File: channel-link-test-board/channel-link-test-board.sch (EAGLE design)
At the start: 60 parts, among them U1 DS90CR217MTD/NOPBMTD48_TEX-L, U2 DS90CR218AMTD/NOPBMTD48_TEX-L

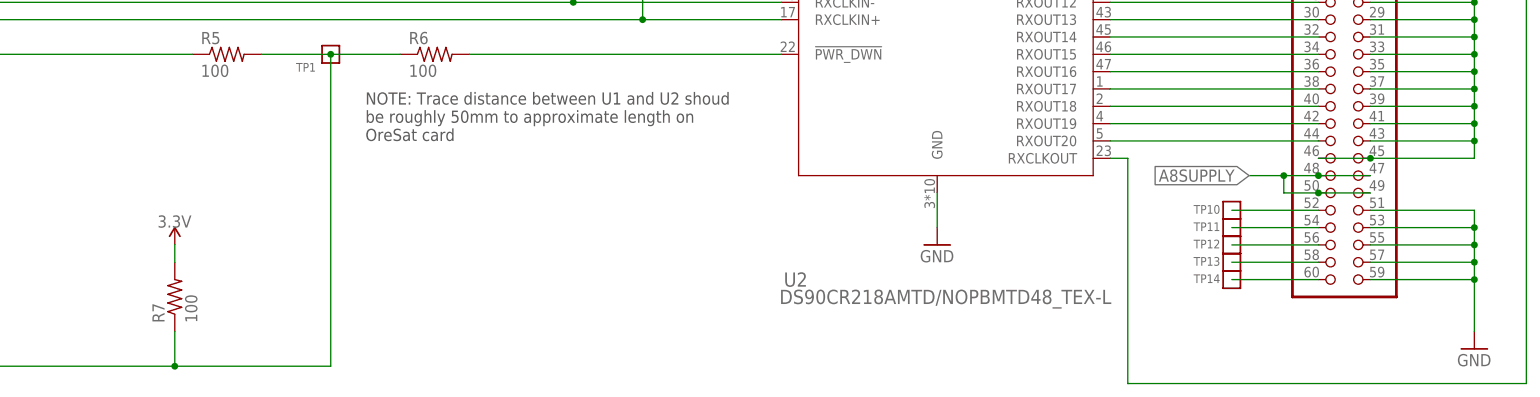
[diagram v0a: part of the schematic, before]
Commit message: minor cleanup, ground stitching, attributes
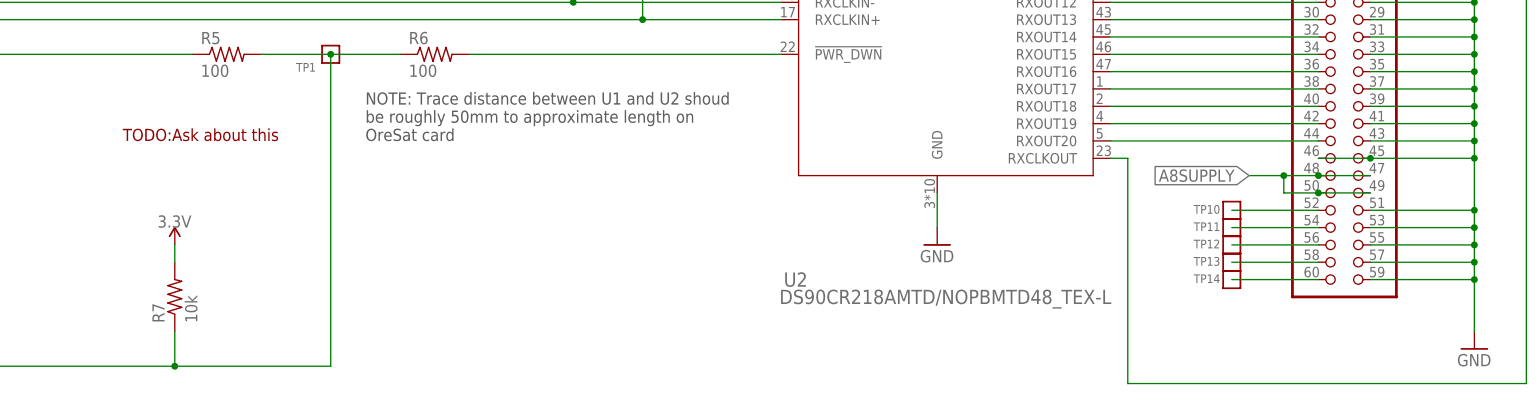
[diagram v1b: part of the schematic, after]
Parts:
- C1, C19, C2, C20, C21, C22, C23, C24, C3, C4, C5, C6: DIS (none) -> Digi-Key; DPN (none) -> 490-6350-1-ND; MFR (none) -> Murata; MPN (none) -> GRM155R71H102KA01J
- C10, C11, C12, C25, C26, C27, C28, C29, C30, C7, C8, C9: DIS (none) -> Digi-Key; DPN (none) -> 399-7842-1-ND; MFR (none) -> Kemet; MPN (none) -> C0603C103M5RACTU
- C13, C14, C15, C16, C17, C18, C31, C32, C33, C34, C35, C36: DIS (none) -> Digi-Key; DPN (none) -> 399-1177-1-ND; MFR (none) -> Kemet; MPN (none) -> C0805C104Z5VACTU
- C37, C38: DIS (none) -> Digi-Key; DPN (none) -> 490-14372-1-ND; MFR (none) -> Murata; MPN (none) -> GRM188R61A106KE69J
- R1, R2, R3, R4: DIS (none) -> Dgi-Key; DPN (none) -> 311-100MCT-ND; MFR (none) -> Yageo; MPN (none) -> RC0201FR-07100RL
- R5, R6: DIS (none) -> Digi-Key; DPN (none) -> 311-100HRCT-ND; MFR (none) -> Yageo; MPN (none) -> RC0603FR-07100RL
- R7: value 100 -> 10k; DIS (none) -> Digi-Key; DPN (none) -> 311-10.0KHRCT-ND; MFR (none) -> Yageo; MPN (none) -> RC0603FR-0710KL
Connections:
- removed net N$46: JP2.1, JP2.11, JP2.13, JP2.15, JP2.17, JP2.19, JP2.21, JP2.23, JP2.25, JP2.27, JP2.29, JP2.3, JP2.31, JP2.33, JP2.35, JP2.37, JP2.39, JP2.41, JP2.43, JP2.45, JP2.46, JP2.5, JP2.7, JP2.9
- net GND: now also JP2.1, JP2.11, JP2.13, JP2.15, JP2.17, JP2.19, JP2.21, JP2.23, JP2.25, JP2.27, JP2.29, JP2.3, JP2.31, JP2.33, JP2.35, JP2.37, JP2.39, JP2.41, JP2.43, JP2.45, JP2.46, JP2.5, JP2.7, JP2.9
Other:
- note added: "TODO:Ask about this"

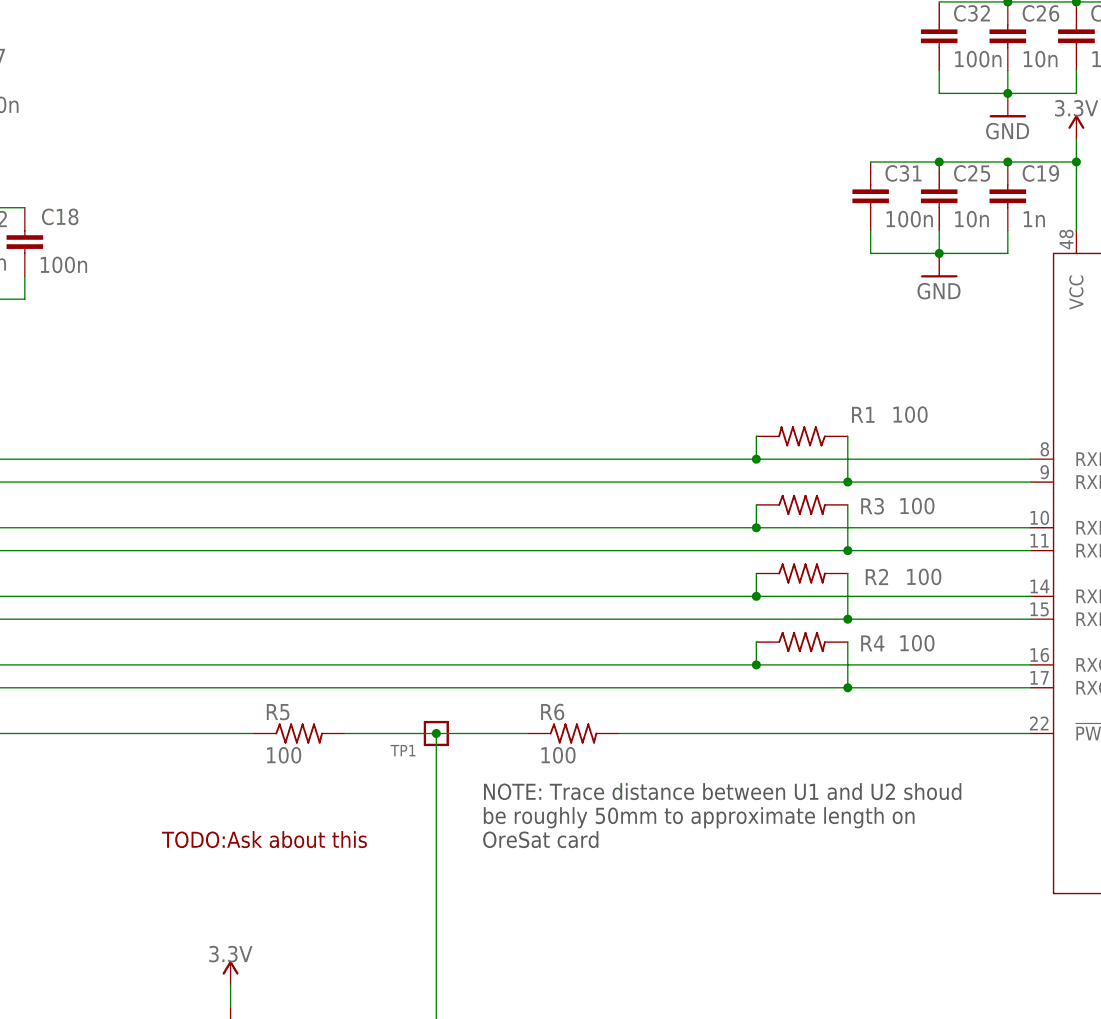
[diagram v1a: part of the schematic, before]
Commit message: moved LVDS lines so I could bypass the LVDS VCC
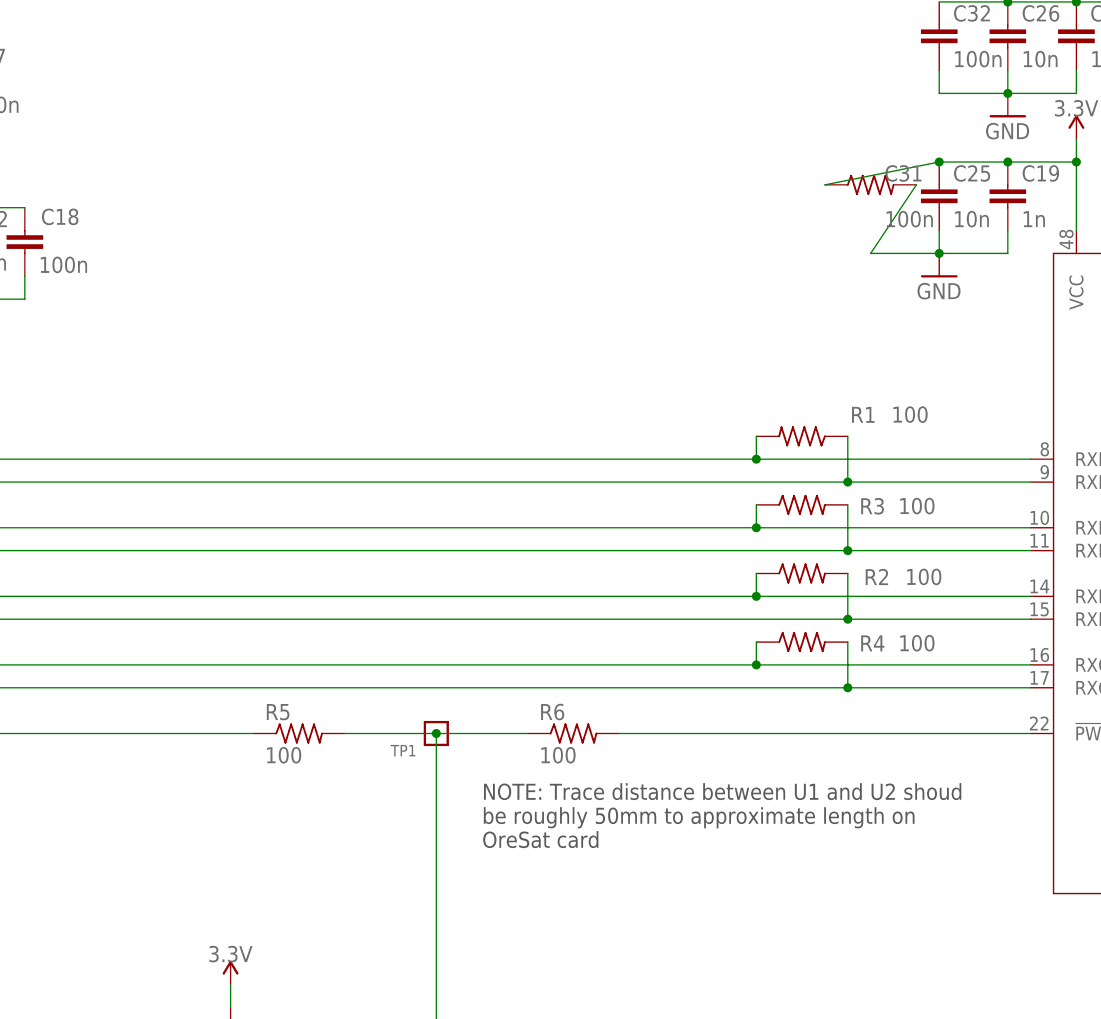
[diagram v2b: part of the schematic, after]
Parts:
- C12, C25: device oresat-rcl:C-EU0603-C-NOSILK -> oresat-rcl:C-EU0402-C-NOSILK
- C14: device oresat-rcl:C-EU0805-C-NOSILK -> oresat-rcl:C-EU0402-C-NOSILK
- C31: device oresat-rcl:C-EU0805-C-NOSILK -> oresat-rcl:R-US_0402-C-NOSILK
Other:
- note removed: "TODO:Ask about this"
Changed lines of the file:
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@@
 <attribute name="MPN" value="C0603C103M5RACTU"/>
 </part>
-<part name="C12" library="oresat-rcl" deviceset="C-EU" device="0603-C-NOSILK" value="10n">
+<part name="C12" library="oresat-rcl" deviceset="C-EU" device="0402-C-NOSILK" value="10n">
 <attribute name="DIS" value="Digi-Key"/>
 <attribute name="DPN" value="399-7842-1-ND"/>
@@
 <attribute name="MPN" value="C0805C104Z5VACTU"/>
 </part>
-<part name="C14" library="oresat-rcl" deviceset="C-EU" device="0805-C-NOSILK" value="100n">
+<part name="C14" library="oresat-rcl" deviceset="C-EU" device="0402-C-NOSILK" value="100n">
 <attribute name="DIS" value="Digi-Key"/>
 <attribute name="DPN" value="399-1177-1-ND"/>
@@
 <attribute name="MPN" value="GRM155R71H102KA01J"/>
 </part>
-<part name="C25" library="oresat-rcl" deviceset="C-EU" device="0603-C-NOSILK" value="10n">
+<part name="C25" library="oresat-rcl" deviceset="C-EU" device="0402-C-NOSILK" value="10n">
 <attribute name="DIS" value="Digi-Key"/>
 <attribute name="DPN" value="399-7842-1-ND"/>
@@
 <attribute name="MPN" value="C0603C103M5RACTU"/>
 </part>
-<part name="C31" library="oresat-rcl" deviceset="C-EU" device="0805-C-NOSILK" value="100n">
+<part name="C31" library="oresat-rcl" deviceset="R-US_" device="0402-C-NOSILK" value="100n">
 <attribute name="DIS" value="Digi-Key"/>
 <attribute name="DPN" value="399-1177-1-ND"/>
@@
 OreSat card</text>
 <text x="182.88" y="231.14" size="1.778" layer="97">Place jumper to determine which connected dev board powers the 3.3V rail</text>
-<text x="193.04" y="132.08" size="1.778" layer="94">TODO:Ask about this</text>
 </plain>
 <instances>
@@
 <attribute name="MFR" x="347.98" y="205.74" size="1.778" layer="96" display="off"/>
 </instance>
-<instance part="C31" gate="CE" x="271.78" y="205.74" smashed="yes">
+<instance part="C31" gate="R" x="271.78" y="205.74" smashed="yes">
 <attribute name="NAME" x="273.304" y="206.121" size="1.778" layer="95"/>
 <attribute name="VALUE" x="273.304" y="201.041" size="1.778" layer="96"/>
@@
 </segment>
 <segment>
-<pinref part="C31" gate="CE" pin="2"/>
-<wire x1="271.78" y1="200.66" x2="271.78" y2="198.12" width="0.1524" layer="91"/>
+<pinref part="C31" gate="R" pin="2"/>
+<wire x1="276.86" y1="205.74" x2="271.78" y2="198.12" width="0.1524" layer="91"/>
 <wire x1="271.78" y1="198.12" x2="279.4" y2="198.12" width="0.1524" layer="91"/>
 <pinref part="C25" gate="CE" pin="2"/>
@@
 <wire x1="279.4" y1="208.28" x2="287.02" y2="208.28" width="0.1524" layer="91"/>
 <junction x="287.02" y="208.28"/>
-<pinref part="C31" gate="CE" pin="1"/>
-<wire x1="271.78" y1="208.28" x2="279.4" y2="208.28" width="0.1524" layer="91"/>
+<pinref part="C31" gate="R" pin="1"/>
+<wire x1="266.7" y1="205.74" x2="279.4" y2="208.28" width="0.1524" layer="91"/>
 <junction x="279.4" y="208.28"/>
 <pinref part="U2" gate="A" pin="VCC"/>

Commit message: ocd fixes
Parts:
- added TP2, TP7: PTR1B2,54, testpad:PTR1B2,54
- C31: device oresat-rcl:R-US_0402-C-NOSILK -> oresat-rcl:C-EU0402-C-NOSILK
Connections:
- net N$1 renamed LVDS0-
- net N$2 renamed LVDS0+
- net N$3 renamed LVDS1-
- net N$4 renamed LVDS1+
- net N$5 renamed LVDS2-
- net N$6 renamed LVDS2+
- net N$7 renamed LVDSCLK-
- net N$8 renamed LVDSCLK+
- net N$30: now also TP2.TP
- net N$66: now also TP7.TP
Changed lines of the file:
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@@
 <attribute name="MPN" value="C0603C103M5RACTU"/>
 </part>
-<part name="C31" library="oresat-rcl" deviceset="R-US_" device="0402-C-NOSILK" value="100n">
+<part name="C31" library="oresat-rcl" deviceset="C-EU" device="0402-C-NOSILK" value="100n">
 <attribute name="DIS" value="Digi-Key"/>
 <attribute name="DPN" value="399-1177-1-ND"/>
@@
 </part>
 <part name="3.3V14" library="oresat-supplies" deviceset="3.3V" device=""/>
+<part name="TP2" library="testpad" library_urn="urn:adsk.eagle:library:385" deviceset="PTR1" device="B2,54" package3d_urn="urn:adsk.eagle:package:27948/1"/>
+<part name="TP7" library="testpad" library_urn="urn:adsk.eagle:library:385" deviceset="PTR1" device="B2,54" package3d_urn="urn:adsk.eagle:package:27948/1"/>
 </parts>
 <sheets>
@@
 <attribute name="MFR" x="347.98" y="205.74" size="1.778" layer="96" display="off"/>
 </instance>
-<instance part="C31" gate="R" x="271.78" y="205.74" smashed="yes">
+<instance part="C31" gate="CE" x="271.78" y="205.74" smashed="yes">
 <attribute name="NAME" x="273.304" y="206.121" size="1.778" layer="95"/>
 <attribute name="VALUE" x="273.304" y="201.041" size="1.778" layer="96"/>
@@
 <attribute name="VALUE" x="198.12" y="119.38" size="1.778" layer="96"/>
 </instance>
+<instance part="TP2" gate="G$1" x="99.06" y="127" smashed="yes">
+<attribute name="NAME" x="98.044" y="120.65" size="1.778" layer="95" rot="R90"/>
+<attribute name="TP_SIGNAL_NAME" x="100.33" y="124.46" size="1.778" layer="97"/>
+</instance>
+<instance part="TP7" gate="G$1" x="370.84" y="93.98" smashed="yes">
+<attribute name="NAME" x="369.824" y="87.63" size="1.778" layer="95" rot="R90"/>
+<attribute name="TP_SIGNAL_NAME" x="372.11" y="91.44" size="1.778" layer="97"/>
+</instance>
 </instances>
 <busses>
 </busses>
 <nets>
-<net name="N$1" class="0">
+<net name="LVDS0-" class="0">
 <segment>
 <pinref part="U1" gate="A" pin="TXOUT0-"/>
@@
 <wire x1="259.08" y1="177.8" x2="259.08" y2="175.26" width="0.1524" layer="91"/>
 <junction x="259.08" y="175.26"/>
-</segment>
-</net>
-<net name="N$2" class="0">
+<label x="165.1" y="175.26" size="1.778" layer="95"/>
+</segment>
+</net>
+<net name="LVDS0+" class="0">
 <segment>
 <pinref part="U1" gate="A" pin="TXOUT0+"/>
@@
 <wire x1="269.24" y1="177.8" x2="269.24" y2="172.72" width="0.1524" layer="91"/>
 <junction x="269.24" y="172.72"/>
-</segment>
-</net>
-<net name="N$3" class="0">
+<label x="165.1" y="172.72" size="1.778" layer="95"/>
+</segment>
+</net>
+<net name="LVDS1-" class="0">
 <segment>
 <pinref part="U1" gate="A" pin="TXOUT1-"/>
@@
 <wire x1="259.08" y1="170.18" x2="259.08" y2="167.64" width="0.1524" layer="91"/>
 <junction x="259.08" y="167.64"/>
-</segment>
-</net>
-<net name="N$4" class="0">
+<label x="165.1" y="167.64" size="1.778" layer="95"/>
+</segment>
+</net>
+<net name="LVDS1+" class="0">
 <segment>
 <pinref part="U1" gate="A" pin="TXOUT1+"/>
@@
 <wire x1="269.24" y1="170.18" x2="269.24" y2="165.1" width="0.1524" layer="91"/>
 <junction x="269.24" y="165.1"/>
-</segment>
-</net>
-<net name="N$5" class="0">
+<label x="165.1" y="165.1" size="1.778" layer="95"/>
+</segment>
+</net>
+<net name="LVDS2-" class="0">
 <segment>
 <pinref part="U1" gate="A" pin="TXOUT2-"/>
@@
 <wire x1="259.08" y1="162.56" x2="259.08" y2="160.02" width="0.1524" layer="91"/>
 <junction x="259.08" y="160.02"/>
-</segment>
-</net>
-<net name="N$6" class="0">
+<label x="165.1" y="160.02" size="1.778" layer="95"/>
+</segment>
+</net>
+<net name="LVDS2+" class="0">
 <segment>
 <pinref part="U2" gate="A" pin="RXIN2+"/>
@@
 <wire x1="269.24" y1="162.56" x2="269.24" y2="157.48" width="0.1524" layer="91"/>
 <junction x="269.24" y="157.48"/>
-</segment>
-</net>
-<net name="N$7" class="0">
+<label x="165.1" y="157.48" size="1.778" layer="95"/>
+</segment>
+</net>
+<net name="LVDSCLK-" class="0">
 <segment>
 <pinref part="U2" gate="A" pin="RXCLKIN-"/>
@@
 <wire x1="259.08" y1="154.94" x2="259.08" y2="152.4" width="0.1524" layer="91"/>
 <junction x="259.08" y="152.4"/>
-</segment>
-</net>
-<net name="N$8" class="0">
+<label x="165.1" y="152.4" size="1.778" layer="95"/>
+</segment>
+</net>
+<net name="LVDSCLK+" class="0">
 <segment>
 <pinref part="U1" gate="A" pin="TXCLK_OUT+"/>
@@
 <wire x1="269.24" y1="154.94" x2="269.24" y2="149.86" width="0.1524" layer="91"/>
 <junction x="269.24" y="149.86"/>
+<label x="165.1" y="149.86" size="1.778" layer="95"/>
 </segment>
 </net>
@@
 </segment>
 <segment>
-<pinref part="C31" gate="R" pin="2"/>
-<wire x1="276.86" y1="205.74" x2="271.78" y2="198.12" width="0.1524" layer="91"/>
+<pinref part="C31" gate="CE" pin="2"/>
+<wire x1="271.78" y1="200.66" x2="271.78" y2="198.12" width="0.1524" layer="91"/>
 <wire x1="271.78" y1="198.12" x2="279.4" y2="198.12" width="0.1524" layer="91"/>
 <pinref part="C25" gate="CE" pin="2"/>
@@
 <wire x1="279.4" y1="208.28" x2="287.02" y2="208.28" width="0.1524" layer="91"/>
 <junction x="287.02" y="208.28"/>
-<pinref part="C31" gate="R" pin="1"/>
-<wire x1="266.7" y1="205.74" x2="279.4" y2="208.28" width="0.1524" layer="91"/>
+<pinref part="C31" gate="CE" pin="1"/>
+<wire x1="271.78" y1="208.28" x2="279.4" y2="208.28" width="0.1524" layer="91"/>
 <junction x="279.4" y="208.28"/>
 <pinref part="U2" gate="A" pin="VCC"/>
@@
 <pinref part="JP1" gate="A" pin="44"/>
 <pinref part="U1" gate="A" pin="TXCLK_IN"/>
-<wire x1="27.94" y1="129.54" x2="111.76" y2="129.54" width="0.1524" layer="91"/>
+<wire x1="27.94" y1="129.54" x2="99.06" y2="129.54" width="0.1524" layer="91"/>
+<pinref part="TP2" gate="G$1" pin="TP"/>
+<wire x1="99.06" y1="129.54" x2="111.76" y2="129.54" width="0.1524" layer="91"/>
+<junction x="99.06" y="129.54"/>
 </segment>
 </net>
@@
 <wire x1="337.82" y1="129.54" x2="340.36" y2="129.54" width="0.1524" layer="91"/>
 <wire x1="340.36" y1="129.54" x2="340.36" y2="96.52" width="0.1524" layer="91"/>
-<wire x1="340.36" y1="96.52" x2="398.78" y2="96.52" width="0.1524" layer="91"/>
+<wire x1="340.36" y1="96.52" x2="370.84" y2="96.52" width="0.1524" layer="91"/>
+<wire x1="370.84" y1="96.52" x2="398.78" y2="96.52" width="0.1524" layer="91"/>
 <wire x1="398.78" y1="96.52" x2="398.78" y2="190.5" width="0.1524" layer="91"/>
 <pinref part="JP2" gate="A" pin="2"/>
 <wire x1="398.78" y1="190.5" x2="368.3" y2="190.5" width="0.1524" layer="91"/>
 <wire x1="368.3" y1="190.5" x2="368.3" y2="185.42" width="0.1524" layer="91"/>
-</segment>
-</net>
+<pinref part="TP7" gate="G$1" pin="TP"/>
+<junction x="370.84" y="96.52"/>
+</segment>
+</net>
